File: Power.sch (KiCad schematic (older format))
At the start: 11 parts

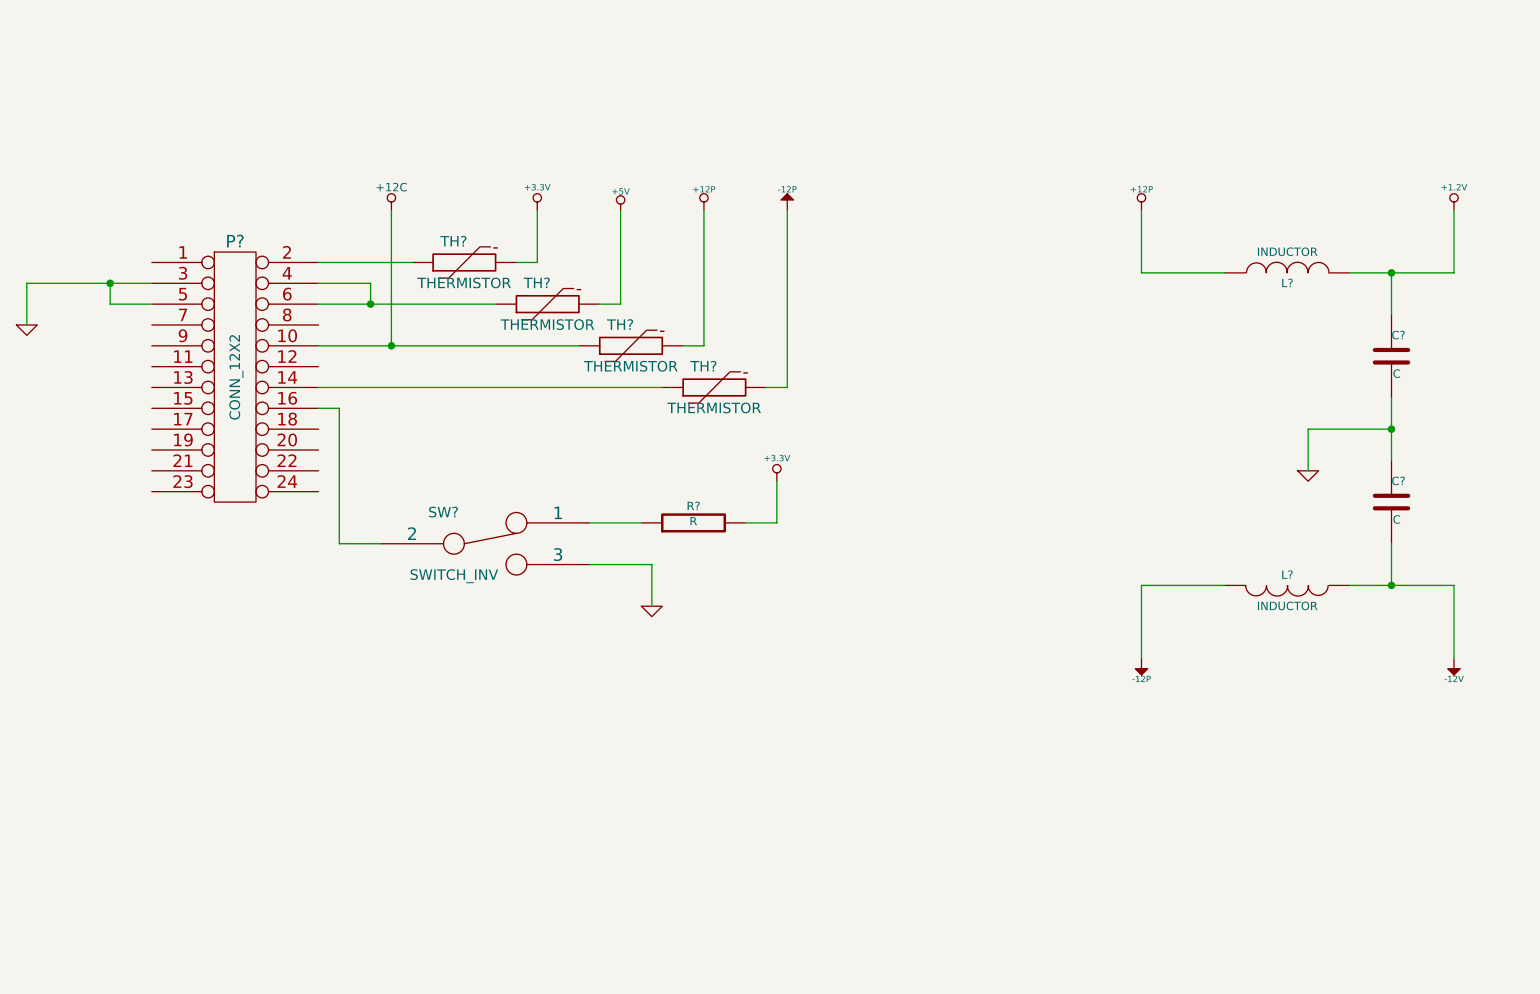
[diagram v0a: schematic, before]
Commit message: Added Relay module footprints.
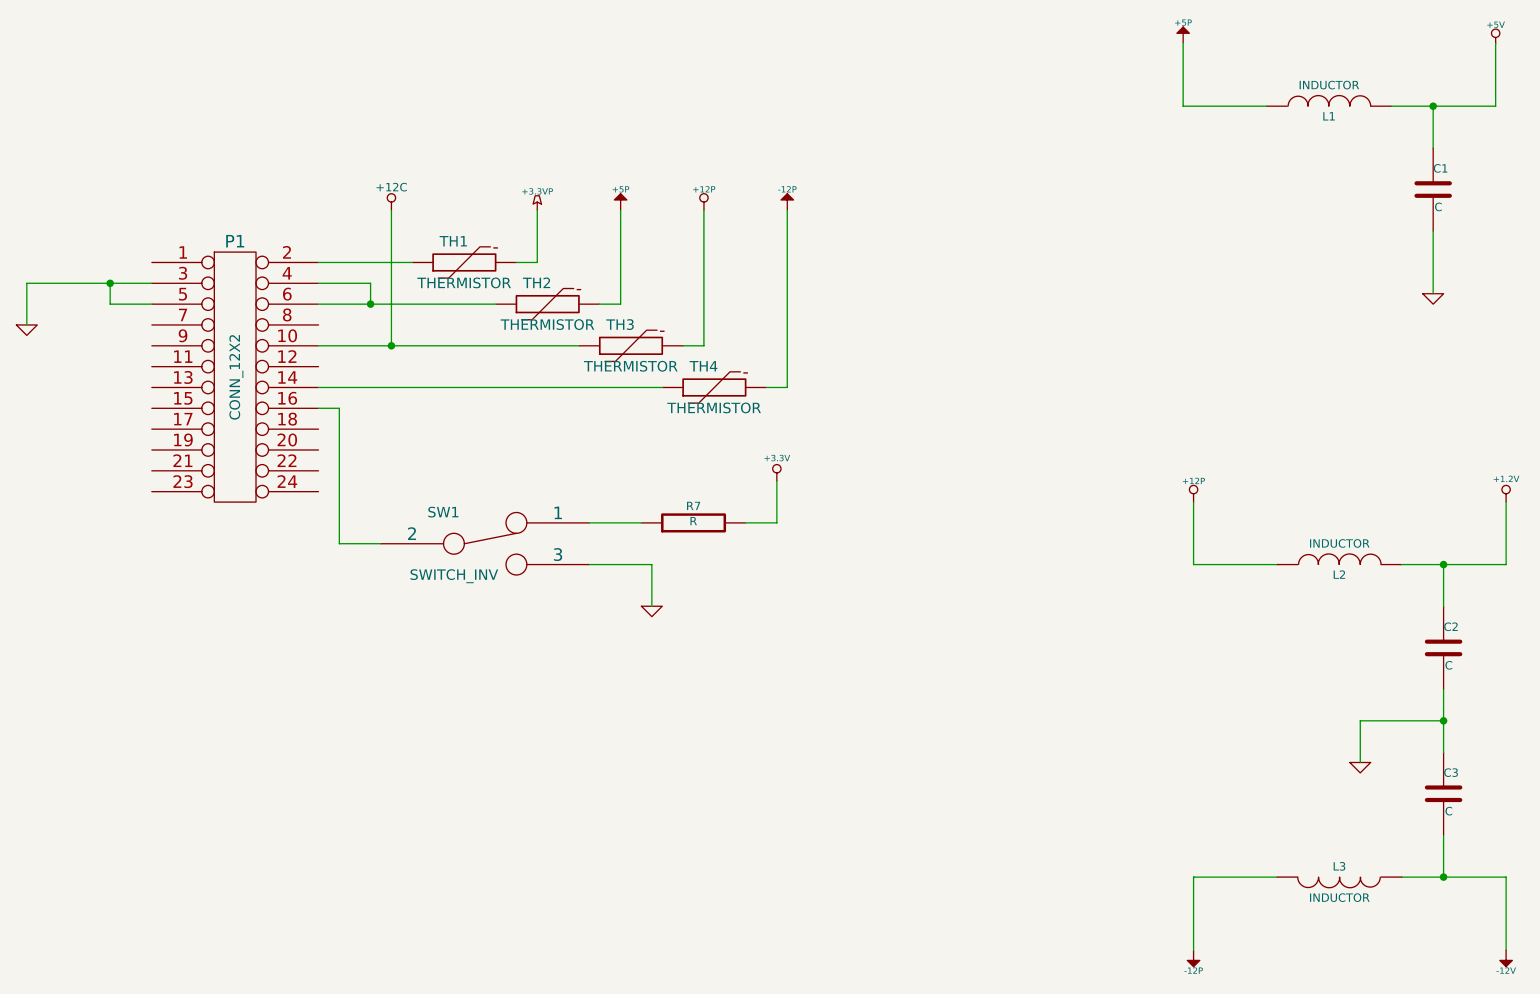
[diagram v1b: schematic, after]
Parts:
- added C1: C, symbol C
- added L1: INDUCTOR, symbol INDUCTOR
- gave numbers to parts that had none: 11
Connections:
- net +3.3V: no longer TH1.2
- net +5V: now also C1.1, L1.2; no longer TH2.2
- net GND: now also C1.2
- new net +3.3VP: TH1.2
- new net +5P: L1.1, TH2.2
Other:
- moved on the sheet: C2, C3, L2, L3

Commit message: Associated and placed thermocouple, terminal, arduino, fan driver, power protection modules.
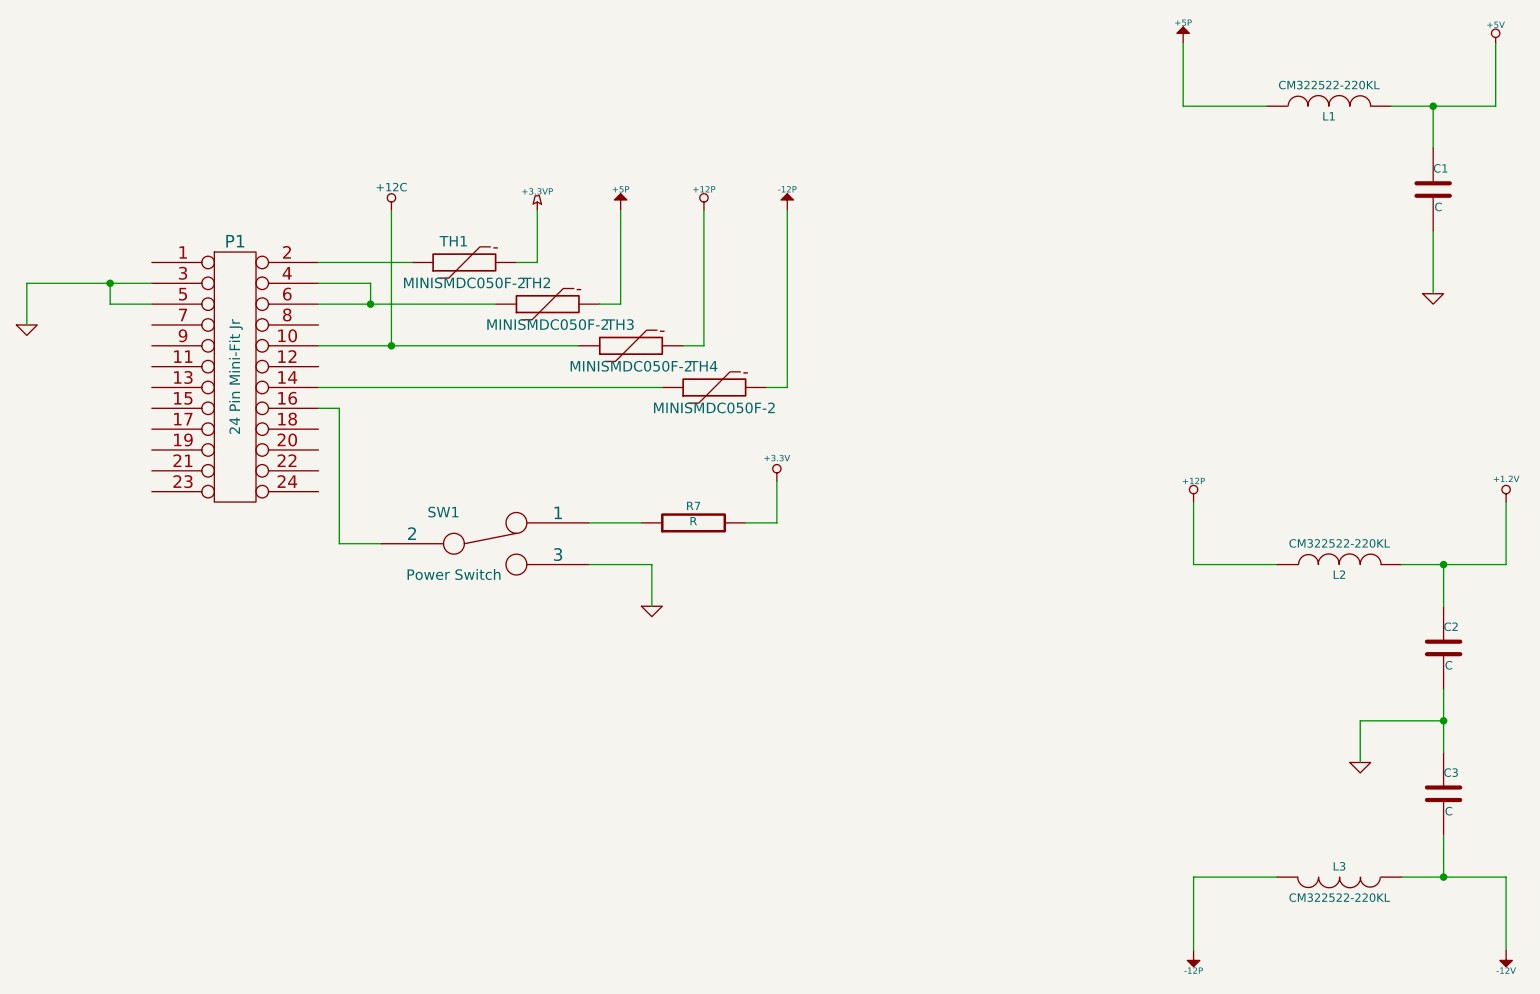
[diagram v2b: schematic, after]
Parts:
- L1, L2, L3: value INDUCTOR -> CM322522-220KL; MFG Part Number (none) -> CM322522-220KL; MFG name (none) -> Bourns Inc
- P1: value CONN_12X2 -> 24 Pin Mini-Fit Jr; MFG Part Number (none) -> 39-30-1240; MFG name (none) -> Molex
- SW1: value SWITCH_INV -> Power Switch; MFG Part Number (none) -> OS102011MA1QN1; MFG name (none) -> C&K Components
- TH1, TH2, TH3, TH4: value THERMISTOR -> MINISMDC050F-2; MFG Part Number (none) -> MINISMDC050F-2; MFG name (none) -> TE Connectivity
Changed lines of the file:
@@
 P 2850 3100
 F 0 "P1" H 2850 3750 60  0000 C CNN
-F 1 "CONN_12X2" V 2850 3100 50  0000 C CNN
+F 1 "24 Pin Mini-Fit Jr" V 2850 3100 50  0000 C CNN
 F 2 "" H 2850 3100 60  0000 C CNN
 F 3 "" H 2850 3100 60  0000 C CNN
+F 4 "Molex" H 2850 3100 60  0001 C CNN "MFG name"
+F 5 "39-30-1240" H 2850 3100 60  0001 C CNN "MFG Part Number"
 	1    2850 3100
 	1    0    0    -1
 $EndComp
 $Comp
-L GND #PWR1
+L GND #PWR01
 U 1 1 52F6A571
 P 1850 2850
-F 0 "#PWR1" H 1850 2850 30  0001 C CNN
+F 0 "#PWR01" H 1850 2850 30  0001 C CNN
 F 1 "GND" H 1850 2780 30  0001 C CNN
 F 2 "" H 1850 2850 60  0000 C CNN
@@
 P 4050 3900
 F 0 "SW1" H 3850 4050 50  0000 C CNN
-F 1 "SWITCH_INV" H 3900 3750 50  0000 C CNN
+F 1 "Power Switch" H 3900 3750 50  0000 C CNN
 F 2 "" H 4050 3900 60  0000 C CNN
 F 3 "" H 4050 3900 60  0000 C CNN
+F 4 "C&K Components" H 4050 3900 60  0001 C CNN "MFG name"
+F 5 "OS102011MA1QN1" H 4050 3900 60  0001 C CNN "MFG Part Number"
 	1    4050 3900
 	1    0    0    -1
@@
 	4900 3150 3250 3150
 $Comp
-L +12P #PWR6
+L +12P #PWR02
 U 1 1 52F6A69C
 P 5100 2300
-F 0 "#PWR6" H 5100 2270 30  0001 C CNN
+F 0 "#PWR02" H 5100 2270 30  0001 C CNN
 F 1 "+12P" H 5100 2400 30  0000 C CNN
 F 2 "" H 5100 2300 60  0000 C CNN
@@
 	5100 2950 5100 2300
 $Comp
-L -12P #PWR8
+L -12P #PWR03
 U 1 1 52F6A72B
 P 5500 2300
-F 0 "#PWR8" H 5500 2430 20  0001 C CNN
+F 0 "#PWR03" H 5500 2430 20  0001 C CNN
 F 1 "-12P" H 5500 2400 30  0000 C CNN
 F 2 "" H 5500 2300 60  0000 C CNN
@@
 	4850 4000 4850 4200
 $Comp
-L GND #PWR5
+L GND #PWR04
 U 1 1 52F6A94F
 P 4850 4200
-F 0 "#PWR5" H 4850 4200 30  0001 C CNN
+F 0 "#PWR04" H 4850 4200 30  0001 C CNN
 F 1 "GND" H 4850 4130 30  0001 C CNN
 F 2 "" H 4850 4200 60  0000 C CNN
@@
 	5300 3800 5450 3800
 $Comp
-L +3.3V #PWR7
+L +3.3V #PWR05
 U 1 1 52F6A9C1
 P 5450 3600
-F 0 "#PWR7" H 5450 3560 30  0001 C CNN
+F 0 "#PWR05" H 5450 3560 30  0001 C CNN
 F 1 "+3.3V" H 5450 3710 30  0000 C CNN
 F 2 "" H 5450 3600 60  0000 C CNN
@@
 	5450 3800 5450 3600
 $Comp
-L +12P #PWR10
+L +12P #PWR06
 U 1 1 52F6AB99
 P 7450 3700
-F 0 "#PWR10" H 7450 3670 30  0001 C CNN
+F 0 "#PWR06" H 7450 3670 30  0001 C CNN
 F 1 "+12P" H 7450 3800 30  0000 C CNN
 F 2 "" H 7450 3700 60  0000 C CNN
@@
 $EndComp
 $Comp
-L -12P #PWR11
+L -12P #PWR07
 U 1 1 52F6ABA4
 P 7450 5850
-F 0 "#PWR11" H 7450 5980 20  0001 C CNN
+F 0 "#PWR07" H 7450 5980 20  0001 C CNN
 F 1 "-12P" H 7450 5950 30  0000 C CNN
 F 2 "" H 7450 5850 60  0000 C CNN
@@
 $EndComp
 $Comp
-L GND #PWR12
+L GND #PWR08
 U 1 1 52F6ABAF
 P 8250 4950
-F 0 "#PWR12" H 8250 4950 30  0001 C CNN
+F 0 "#PWR08" H 8250 4950 30  0001 C CNN
 F 1 "GND" H 8250 4880 30  0001 C CNN
 F 2 "" H 8250 4950 60  0000 C CNN
@@
 	1    8250 4950
 	1    0    0    -1
-$EndComp
-$Comp
-L INDUCTOR L2
-U 1 1 52F6ABBC
-P 8150 4000
-F 0 "L2" V 8100 4000 40  0000 C CNN
-F 1 "INDUCTOR" V 8250 4000 40  0000 C CNN
-F 2 "" H 8150 4000 60  0000 C CNN
-F 3 "" H 8150 4000 60  0000 C CNN
-	1    8150 4000
-	0    -1   -1   0
-$EndComp
-$Comp
-L INDUCTOR L3
-U 1 1 52F6ABCE
-P 8150 5500
-F 0 "L3" V 8100 5500 40  0000 C CNN
-F 1 "INDUCTOR" V 8250 5500 40  0000 C CNN
-F 2 "" H 8150 5500 60  0000 C CNN
-F 3 "" H 8150 5500 60  0000 C CNN
-	1    8150 5500
-	0    1    1    0
 $EndComp
 $Comp
@@
 Connection ~ 8650 4750
 $Comp
-L +1.2V #PWR15
+L +1.2V #PWR09
 U 1 1 52F6AD0F
 P 8950 3700
-F 0 "#PWR15" H 8950 3840 20  0001 C CNN
+F 0 "#PWR09" H 8950 3840 20  0001 C CNN
 F 1 "+1.2V" H 8950 3810 30  0000 C CNN
 F 2 "" H 8950 3700 60  0000 C CNN
@@
 $EndComp
 $Comp
-L -12V #PWR16
+L -12V #PWR010
 U 1 1 52F6AD23
 P 8950 5850
-F 0 "#PWR16" H 8950 5980 20  0001 C CNN
+F 0 "#PWR010" H 8950 5980 20  0001 C CNN
 F 1 "-12V" H 8950 5950 30  0000 C CNN
 F 2 "" H 8950 5850 60  0000 C CNN
@@
 P 3950 2550
 F 0 "TH1" V 4050 2600 50  0000 C CNN
-F 1 "THERMISTOR" V 3850 2550 50  0000 C CNN
+F 1 "MINISMDC050F-2" V 3850 2550 50  0000 C CNN
 F 2 "" H 3950 2550 60  0000 C CNN
 F 3 "" H 3950 2550 60  0000 C CNN
+F 4 "TE Connectivity" H 3950 2550 60  0001 C CNN "MFG name"
+F 5 "MINISMDC050F-2" H 3950 2550 60  0001 C CNN "MFG Part Number"
 	1    3950 2550
-	0    -1   -1   0
-$EndComp
-$Comp
-L THERMISTOR TH2
-U 1 1 52F96A6D
-P 4350 2750
-F 0 "TH2" V 4450 2800 50  0000 C CNN
-F 1 "THERMISTOR" V 4250 2750 50  0000 C CNN
-F 2 "" H 4350 2750 60  0000 C CNN
-F 3 "" H 4350 2750 60  0000 C CNN
-	1    4350 2750
-	0    -1   -1   0
-$EndComp
-$Comp
-L THERMISTOR TH3
-U 1 1 52F96A78
-P 4750 2950
-F 0 "TH3" V 4850 3000 50  0000 C CNN
-F 1 "THERMISTOR" V 4650 2950 50  0000 C CNN
-F 2 "" H 4750 2950 60  0000 C CNN
-F 3 "" H 4750 2950 60  0000 C CNN
-	1    4750 2950
-	0    -1   -1   0
-$EndComp
-$Comp
-L THERMISTOR TH4
-U 1 1 52F96A83
-P 5150 3150
-F 0 "TH4" V 5250 3200 50  0000 C CNN
-F 1 "THERMISTOR" V 5050 3150 50  0000 C CNN
-F 2 "" H 5150 3150 60  0000 C CNN
-F 3 "" H 5150 3150 60  0000 C CNN
-	1    5150 3150
 	0    -1   -1   0
 $EndComp
@@
 Connection ~ 3600 2950
 $Comp
-L +12C #PWR2
+L +12C #PWR011
 U 1 1 52F96AC6
 P 3600 2300
-F 0 "#PWR2" H 3600 2270 30  0001 C CNN
+F 0 "#PWR011" H 3600 2270 30  0001 C CNN
 F 1 "+12C" H 3600 2410 40  0000 C CNN
 F 2 "" H 3600 2300 60  0000 C CNN
@@
 $EndComp
 $Comp
-L GND #PWR13
+L GND #PWR012
 U 1 1 53025E09
 P 8600 2700
-F 0 "#PWR13" H 8600 2700 30  0001 C CNN
+F 0 "#PWR012" H 8600 2700 30  0001 C CNN
 F 1 "GND" H 8600 2630 30  0001 C CNN
 F 2 "" H 8600 2700 60  0000 C CNN
@@
 P 8100 1800
 F 0 "L1" V 8050 1800 40  0000 C CNN
-F 1 "INDUCTOR" V 8200 1800 40  0000 C CNN
+F 1 "CM322522-220KL" V 8200 1800 40  0000 C CNN
 F 2 "" H 8100 1800 60  0000 C CNN
 F 3 "" H 8100 1800 60  0000 C CNN
+F 4 "Bourns Inc" H 8100 1800 60  0001 C CNN "MFG name"
+F 5 "CM322522-220KL" H 8100 1800 60  0001 C CNN "MFG Part Number"
 	1    8100 1800
 	0    -1   -1   0
@@
 	7400 1800 7400 1500
 $Comp
-L +5V #PWR14
+L +5V #PWR013
 U 1 1 53026091
 P 8900 1500
-F 0 "#PWR14" H 8900 1590 20  0001 C CNN
+F 0 "#PWR013" H 8900 1590 20  0001 C CNN
 F 1 "+5V" H 8900 1590 30  0000 C CNN
 F 2 "" H 8900 1500 60  0000 C CNN
@@
 $EndComp
 $Comp
-L +3.3VP #PWR3
+L +3.3VP #PWR014
 U 1 1 5302613A
 P 4300 2300
-F 0 "#PWR3" H 4350 2330 20  0001 C CNN
+F 0 "#PWR014" H 4350 2330 20  0001 C CNN
 F 1 "+3.3VP" H 4300 2390 30  0000 C CNN
 F 2 "" H 4300 2300 60  0000 C CNN
@@
 	1    0    0    -1
 $EndComp
+$Comp
+L THERMISTOR TH2
+U 1 1 530A5590
+P 4350 2750
+F 0 "TH2" V 4450 2800 50  0000 C CNN
+F 1 "MINISMDC050F-2" V 4250 2750 50  0000 C CNN
+F 2 "" H 4350 2750 60  0000 C CNN
+F 3 "" H 4350 2750 60  0000 C CNN
+F 4 "TE Connectivity" H 4350 2750 60  0001 C CNN "MFG name"
+F 5 "MINISMDC050F-2" H 4350 2750 60  0001 C CNN "MFG Part Number"
+	1    4350 2750
+	0    -1   -1   0
+$EndComp
+$Comp
+L THERMISTOR TH3
+U 1 1 530A559F
+P 4750 2950
+F 0 "TH3" V 4850 3000 50  0000 C CNN
+F 1 "MINISMDC050F-2" V 4650 2950 50  0000 C CNN
+F 2 "" H 4750 2950 60  0000 C CNN
+F 3 "" H 4750 2950 60  0000 C CNN
+F 4 "TE Connectivity" H 4750 2950 60  0001 C CNN "MFG name"
+F 5 "MINISMDC050F-2" H 4750 2950 60  0001 C CNN "MFG Part Number"
+	1    4750 2950
+	0    -1   -1   0
+$EndComp
+$Comp
+L THERMISTOR TH4
+U 1 1 530A55AE
+P 5150 3150
+F 0 "TH4" V 5250 3200 50  0000 C CNN
+F 1 "MINISMDC050F-2" V 5050 3150 50  0000 C CNN
+F 2 "" H 5150 3150 60  0000 C CNN
+F 3 "" H 5150 3150 60  0000 C CNN
+F 4 "TE Connectivity" H 5150 3150 60  0001 C CNN "MFG name"
+F 5 "MINISMDC050F-2" H 5150 3150 60  0001 C CNN "MFG Part Number"
+	1    5150 3150
+	0    -1   -1   0
+$EndComp
+$Comp
+L INDUCTOR L2
+U 1 1 530A5619
+P 8150 4000
+F 0 "L2" V 8100 4000 40  0000 C CNN
+F 1 "CM322522-220KL" V 8250 4000 40  0000 C CNN
+F 2 "" H 8150 4000 60  0000 C CNN
+F 3 "" H 8150 4000 60  0000 C CNN
+F 4 "Bourns Inc" H 8150 4000 60  0001 C CNN "MFG name"
+F 5 "CM322522-220KL" H 8150 4000 60  0001 C CNN "MFG Part Number"
+	1    8150 4000
+	0    -1   -1   0
+$EndComp
+$Comp
+L INDUCTOR L3
+U 1 1 530A5628
+P 8150 5500
+F 0 "L3" V 8100 5500 40  0000 C CNN
+F 1 "CM322522-220KL" V 8250 5500 40  0000 C CNN
+F 2 "" H 8150 5500 60  0000 C CNN
+F 3 "" H 8150 5500 60  0000 C CNN
+F 4 "Bourns Inc" H 8150 5500 60  0001 C CNN "MFG name"
+F 5 "CM322522-220KL" H 8150 5500 60  0001 C CNN "MFG Part Number"
+	1    8150 5500
+	0    1    1    0
+$EndComp
 $EndSCHEMATC

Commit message: Layout sessions 1-4.
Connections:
- net +3.3VP is gone; now on net +3.3V: TH1.2
- net at P1.12 (P12): now also P1.2 (P2), TH1.1
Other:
- moved on the sheet: TH1
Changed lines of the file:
@@
 $EndComp
 Wire Wire Line
-	3250 2550 3700 2550
-Wire Wire Line
-	4200 2550 4300 2550
-Wire Wire Line
-	4300 2550 4300 2300
+	3250 2550 3900 2550
+Wire Wire Line
+	4400 2550 4450 2550
+Wire Wire Line
+	4450 2550 4450 2300
 Wire Wire Line
 	3250 2650 3500 2650
@@
 L THERMISTOR TH1
 U 1 1 52F96A4C
-P 3950 2550
-F 0 "TH1" V 4050 2600 50  0000 C CNN
-F 1 "MINISMDC050F-2" V 3850 2550 50  0000 C CNN
-F 2 "" H 3950 2550 60  0000 C CNN
-F 3 "" H 3950 2550 60  0000 C CNN
-F 4 "TE Connectivity" H 3950 2550 60  0001 C CNN "MFG name"
-F 5 "MINISMDC050F-2" H 3950 2550 60  0001 C CNN "MFG Part Number"
-	1    3950 2550
-	0    -1   -1   0
-$EndComp
-Wire Wire Line
-	3600 2950 3600 2300
+P 4150 2550
+F 0 "TH1" V 4250 2600 50  0000 C CNN
+F 1 "MINISMDC050F-2" V 4050 2550 50  0000 C CNN
+F 2 "" H 4150 2550 60  0000 C CNN
+F 3 "" H 4150 2550 60  0000 C CNN
+F 4 "TE Connectivity" H 4150 2550 60  0001 C CNN "MFG name"
+F 5 "MINISMDC050F-2" H 4150 2550 60  0001 C CNN "MFG Part Number"
+	1    4150 2550
+	0    -1   -1   0
+$EndComp
 Connection ~ 3600 2950
 $Comp
@@
 F 3 "" H 4700 2300 60  0000 C CNN
 	1    4700 2300
-	1    0    0    -1
-$EndComp
-$Comp
-L +3.3VP #PWR014
-U 1 1 5302613A
-P 4300 2300
-F 0 "#PWR014" H 4350 2330 20  0001 C CNN
-F 1 "+3.3VP" H 4300 2390 30  0000 C CNN
-F 2 "" H 4300 2300 60  0000 C CNN
-F 3 "" H 4300 2300 60  0000 C CNN
-	1    4300 2300
 	1    0    0    -1
 $EndComp
@@
 	0    1    1    0
 $EndComp
+$Comp
+L +3.3V #PWR014
+U 1 1 53123FE6
+P 4450 2300
+F 0 "#PWR014" H 4450 2260 30  0001 C CNN
+F 1 "+3.3V" H 4450 2410 30  0000 C CNN
+F 2 "" H 4450 2300 60  0000 C CNN
+F 3 "" H 4450 2300 60  0000 C CNN
+	1    4450 2300
+	1    0    0    -1
+$EndComp
+Wire Wire Line
+	3250 3050 3750 3050
+Wire Wire Line
+	3750 3050 3750 2550
+Connection ~ 3750 2550
+Wire Wire Line
+	3600 2300 3600 2950
 $EndSCHEMATC
